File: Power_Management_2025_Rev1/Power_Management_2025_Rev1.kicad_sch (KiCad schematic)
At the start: 100 parts, among them J1 RJ45_LED_Shielded, Q1 BSS138, Q2 IPB180N10S4-02, Q3 IPB180N10S4-02, Q4 IPB180N10S4-02, U1 Teensy4.1_DEV-16771, U10 LT1910, U11 LT1910, U12 PKE3316ZPI, U13 PKE3316ZPI, U14 LT1910, U2 OKI-78SR-3.3_1.5-W36-C, U3 ACS756xCB-050B-PFF, U4 Opamp_Dual, U5 Opamp_Dual, U6 Opamp_Dual

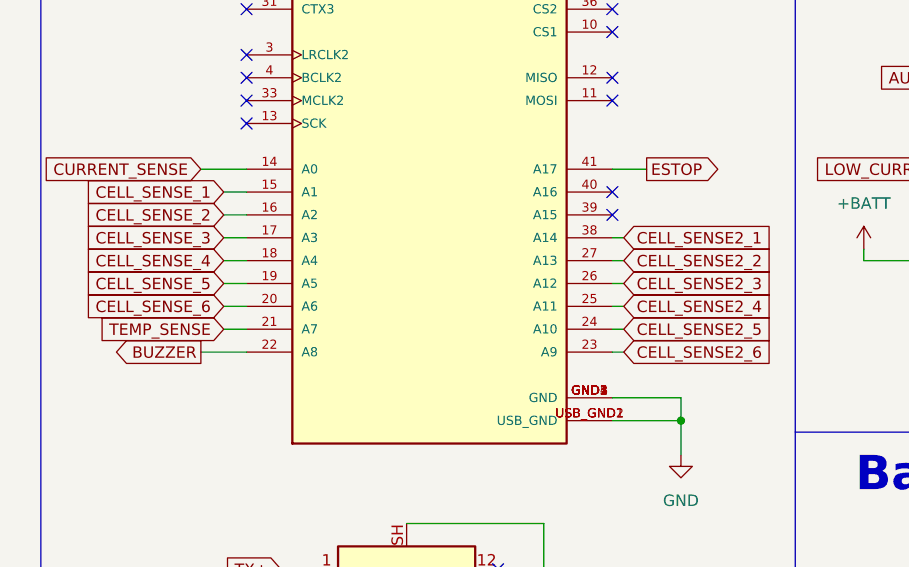
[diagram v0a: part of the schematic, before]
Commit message: Tracing
made a few more traces with the buzzer and cap bank
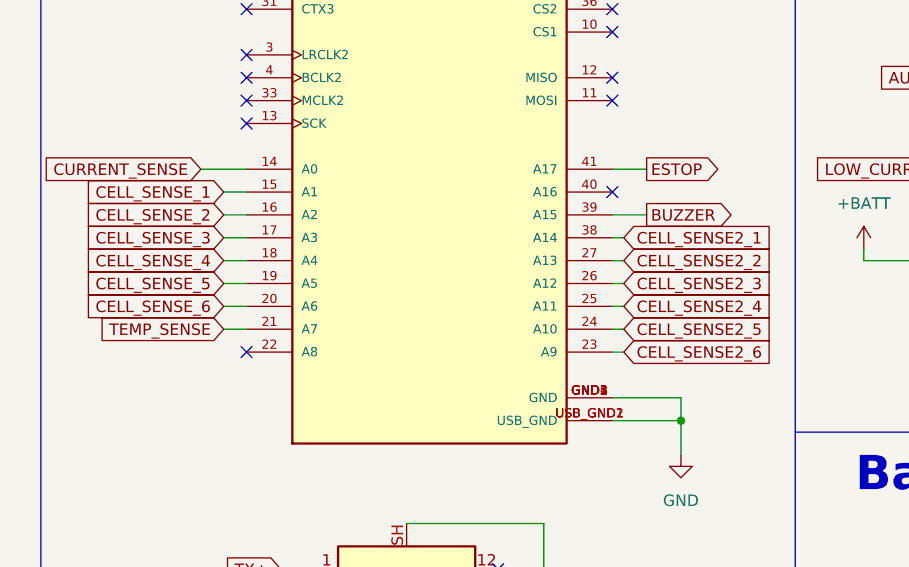
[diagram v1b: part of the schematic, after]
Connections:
- net BUZZER: now also U1.39 (A15); no longer U1.22 (A8)
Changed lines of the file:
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@@
 	)
 	(no_connect
-		(at 74.93 100.33)
-	)
-	(no_connect
 		(at 62.23 139.7)
 	)
@@
 	)
 	(no_connect
+		(at 34.29 115.57)
+	)
+	(no_connect
 		(at 74.93 57.15)
 	)
@@
 	(wire
 		(pts
+			(xy 74.93 100.33) (xy 78.74 100.33)
+		)
+		(stroke
+			(width 0)
+			(type default)
+		)
+	)
+	(wire
+		(pts
 			(xy 278.13 228.6) (xy 278.13 234.95)
 		)
@@
 	(wire
 		(pts
-			(xy 29.21 115.57) (xy 34.29 115.57)
-		)
-		(stroke
-			(width 0)
-			(type default)
-		)
-	)
-	(wire
-		(pts
 			(xy 337.82 224.79) (xy 336.55 224.79)
 		)
@@
 	(global_label "BUZZER"
 		(shape output)
-		(at 29.21 115.57 180)
+		(at 78.74 100.33 0)
 		(fields_autoplaced yes)
 		(effects
@@
 				(size 1.27 1.27)
 			)
-			(justify right)
+			(justify left)
 		)
 		(property "Intersheetrefs" "${INTERSHEET_REFS}"
-			(at 18.7863 115.57 0)
+			(at 89.1637 100.33 0)
 			(effects
 				(font
 					(size 1.27 1.27)
 				)
-				(justify right)
+				(justify left)
 				(hide yes)
 			)

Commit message: More tracework
Made corrections to schematic and did more tracework on PCB
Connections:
- net C_SENSE is gone; now on net CURRENT_SENSE: U3.3 (VIOUT)
- net +BATT: no longer C1.1, C12.1, C14.1, C9.1, F1.1, Q2.4 (D), Q3.4 (D), Q4.4 (D), R35.1, U10.6 (SENSE), U10.8 (V+), U11.6 (SENSE), U11.8 (V+), U12.3 (VIN+), U13.3 (VIN+), U14.6 (SENSE), U14.8 (V+), U2.1 (IN), U3.4 (IP+), U4.8 (V+), U5.8 (V+), U6.8 (V+)
- net IP+: now reaches C4.1, C5.1, C6.1, C7.1, D1.1 (K), F1.2
- net IP+: now also U3.4 (IP+)
- net FF_MOTOR: now reaches U1.22 (A8)
- net FF_MOTOR: now also R28.1
- net FF_LC: now reaches U1.40 (A16)
- net FF_LC: now also R27.1
- removed net +5V: R2.1, R27.1, R28.1
- net ESTOP renamed FF_AUX
- net FF_AUX: now also R2.1
- net PACK_OUT renamed IP-
- net IP-: now also C1.1, C12.1, C14.1, C9.1, F1.1, Q2.4 (D), Q3.4 (D), Q4.4 (D), R35.1, U10.6 (SENSE), U10.8 (V+), U11.6 (SENSE), U11.8 (V+), U12.3 (VIN+), U13.3 (VIN+), U14.6 (SENSE), U14.8 (V+), U2.1 (IN), U4.8 (V+), U5.8 (V+), U6.8 (V+)
- no-connect marks 37 -> 35
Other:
- moved on the sheet: C1, C12, C2, C9, Q2, Q4, U10, U14, U2

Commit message: Pushing opamp new numbers
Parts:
- R10, R11, R14, R15, R18, R19, R22, R23, R26, R4, R6, R7: value 36.5k -> 39k
- R12, R13, R16, R17, R20, R21, R24, R25, R3, R5, R8, R9: value 46.4k -> 47k
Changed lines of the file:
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@@
 			)
 		)
-		(property "Value" "36.5k"
+		(property "Value" "39k"
 			(at 203.2 190.754 90)
 			(effects
@@
 			)
 		)
-		(property "Value" "36.5k"
+		(property "Value" "39k"
 			(at 272.034 177.8 90)
 			(effects
@@
 			)
 		)
-		(property "Value" "46.4k"
+		(property "Value" "47k"
 			(at 292.1 197.104 90)
 			(effects
@@
 			)
 		)
-		(property "Value" "46.4k"
+		(property "Value" "47k"
 			(at 115.824 189.484 90)
 			(effects
@@
 			)
 		)
-		(property "Value" "46.4k"
+		(property "Value" "47k"
 			(at 214.63 190.5 90)
 			(effects
@@
 			)
 		)
-		(property "Value" "46.4k"
+		(property "Value" "47k"
 			(at 252.73 192.024 90)
 			(effects
@@
 			)
 		)
-		(property "Value" "46.4k"
+		(property "Value" "47k"
 			(at 182.88 193.294 90)
 			(effects
@@
 			)
 		)
-		(property "Value" "36.5k"
+		(property "Value" "39k"
 			(at 306.07 179.324 90)
 			(effects
@@
 			)
 		)
-		(property "Value" "36.5k"
+		(property "Value" "39k"
 			(at 196.85 176.784 90)
 			(effects
@@
 			)
 		)
-		(property "Value" "46.4k"
+		(property "Value" "47k"
 			(at 287.02 194.564 90)
 			(effects
@@
 			)
 		)
-		(property "Value" "36.5k"
+		(property "Value" "39k"
 			(at 166.37 189.23 90)
 			(effects
@@
 			)
 		)
-		(property "Value" "46.4k"
+		(property "Value" "47k"
 			(at 145.034 188.214 90)
 			(effects
@@
 			)
 		)
-		(property "Value" "46.4k"
+		(property "Value" "47k"
 			(at 177.8 190.754 90)
 			(effects
@@
 			)
 		)
-		(property "Value" "36.5k"
+		(property "Value" "39k"
 			(at 233.68 176.53 90)
 			(effects
@@
 			)
 		)
-		(property "Value" "36.5k"
+		(property "Value" "39k"
 			(at 275.844 193.294 90)
 			(effects
@@
 			)
 		)
-		(property "Value" "46.4k"
+		(property "Value" "47k"
 			(at 219.71 193.294 90)
 			(effects
@@
 			)
 		)
-		(property "Value" "36.5k"
+		(property "Value" "39k"
 			(at 129.794 172.974 90)
 			(effects
@@
 			)
 		)
-		(property "Value" "46.4k"
+		(property "Value" "47k"
 			(at 149.86 190.754 90)
 			(effects
@@
 			)
 		)
-		(property "Value" "46.4k"
+		(property "Value" "47k"
 			(at 257.81 194.564 90)
 			(effects
@@
 			)
 		)
-		(property "Value" "36.5k"
+		(property "Value" "39k"
 			(at 241.3 192.024 90)
 			(effects
@@
 			)
 		)
-		(property "Value" "46.4k"
+		(property "Value" "47k"
 			(at 110.744 186.944 90)
 			(effects
@@
 			)
 		)
-		(property "Value" "36.5k"
+		(property "Value" "39k"
 			(at 133.604 188.214 90)
 			(effects
@@
 			)
 		)
-		(property "Value" "36.5k"
+		(property "Value" "39k"
 			(at 99.314 186.944 90)
 			(effects
@@
 			)
 		)
-		(property "Value" "36.5k"
+		(property "Value" "39k"
 			(at 163.83 174.244 90)
 			(effects

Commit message: Rearranged component
We Made power planes
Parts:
- C1, C11, C12, C13, C14, C2, C9: footprint Capacitor_THT:CP_Radial_D5.0mm_P2.00mm -> Capacitor_SMD:C_1206_3216Metric_Pad1.33x1.80mm_HandSolder
- C10, C8: footprint Capacitor_THT:CP_Radial_Tantal_D5.0mm_P5.00mm -> Capacitor_THT:CP_Radial_D5.0mm_P2.00mm
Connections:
- net +BATT is gone; now on net IP+: Conn1.4 (PV+), Conn19.4 (PV+)
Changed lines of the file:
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@@
 		)
 	)
+	(global_label "IP+"
+		(shape output)
+		(at 33.02 189.23 90)
+		(fields_autoplaced yes)
+		(effects
+			(font
+				(size 1.27 1.27)
+			)
+			(justify left)
+		)
+		(property "Intersheetrefs" "${INTERSHEET_REFS}"
+			(at 33.02 182.7976 90)
+			(effects
+				(font
+					(size 1.27 1.27)
+				)
+				(justify left)
+				(hide yes)
+			)
+		)
+	)
 	(global_label "CELL4"
 		(shape input)
@@
 		)
 	)
+	(global_label "IP+"
+		(shape output)
+		(at 59.69 187.96 90)
+		(fields_autoplaced yes)
+		(effects
+			(font
+				(size 1.27 1.27)
+			)
+			(justify left)
+		)
+		(property "Intersheetrefs" "${INTERSHEET_REFS}"
+			(at 59.69 181.5276 90)
+			(effects
+				(font
+					(size 1.27 1.27)
+				)
+				(justify left)
+				(hide yes)
+			)
+		)
+	)
 	(global_label "BUZZER"
 		(shape output)
@@
 			)
 		)
-		(property "Footprint" "Capacitor_THT:CP_Radial_D5.0mm_P2.00mm"
+		(property "Footprint" "Capacitor_SMD:C_1206_3216Metric_Pad1.33x1.80mm_HandSolder"
 			(at 372.11 241.3 0)
 			(effects
@@
 			)
 		)
-		(property "Footprint" "Capacitor_THT:CP_Radial_D5.0mm_P2.00mm"
+		(property "Footprint" "Capacitor_SMD:C_1206_3216Metric_Pad1.33x1.80mm_HandSolder"
 			(at 307.0352 48.26 0)
 			(effects
@@
 			)
 		)
-		(property "Footprint" "Capacitor_THT:CP_Radial_D5.0mm_P2.00mm"
+		(property "Footprint" "Capacitor_SMD:C_1206_3216Metric_Pad1.33x1.80mm_HandSolder"
 			(at 278.13 260.35 0)
 			(effects
@@
 			)
 		)
-		(property "Footprint" "Capacitor_THT:CP_Radial_D5.0mm_P2.00mm"
+		(property "Footprint" "Capacitor_SMD:C_1206_3216Metric_Pad1.33x1.80mm_HandSolder"
 			(at 322.2752 48.26 0)
 			(effects
@@
 			)
 		)
-		(property "Footprint" "Capacitor_THT:CP_Radial_Tantal_D5.0mm_P5.00mm"
+		(property "Footprint" "Capacitor_THT:CP_Radial_D5.0mm_P2.00mm"
 			(at 360.9848 96.52 0)
 			(effects
@@
 	)
 	(symbol
-		(lib_id "power:+BATT")
-		(at 33.02 189.23 0)
-		(unit 1)
-		(exclude_from_sim no)
-		(in_bom yes)
-		(on_board yes)
-		(dnp no)
-		(fields_autoplaced yes)
-		(property "Reference" "#PWR01"
-			(at 33.02 193.04 0)
-			(effects
-				(font
-					(size 1.27 1.27)
-				)
-				(hide yes)
-			)
-		)
-		(property "Value" "+BATT"
-			(at 33.02 184.15 0)
-			(effects
-				(font
-					(size 1.27 1.27)
-				)
-			)
-		)
-		(property "Footprint" ""
-			(at 33.02 189.23 0)
-			(effects
-				(font
-					(size 1.27 1.27)
-				)
-				(hide yes)
-			)
-		)
-		(property "Datasheet" ""
-			(at 33.02 189.23 0)
-			(effects
-				(font
-					(size 1.27 1.27)
-				)
-				(hide yes)
-			)
-		)
-		(property "Description" "Power symbol creates a global label with name \"+BATT\""
-			(at 33.02 189.23 0)
-			(effects
-				(font
-					(size 1.27 1.27)
-				)
-				(hide yes)
-			)
-		)
-		(pin "1"
-		)
-		(instances
-			(project ""
-				(path "/e068baf1-d1f0-499a-9461-2503f4f0f679"
-					(reference "#PWR01")
-					(unit 1)
-				)
-			)
-		)
-	)
-	(symbol
 		(lib_id "MRDT_Connectors:AndersonPP")
 		(at 201.93 50.8 0)
@@
 			)
 		)
-		(property "Footprint" "Capacitor_THT:CP_Radial_Tantal_D5.0mm_P5.00mm"
+		(property "Footprint" "Capacitor_THT:CP_Radial_D5.0mm_P2.00mm"
 			(at 354.6348 163.83 0)
 			(effects
@@
 			)
 		)
-		(property "Footprint" "Capacitor_THT:CP_Radial_D5.0mm_P2.00mm"
+		(property "Footprint" "Capacitor_SMD:C_1206_3216Metric_Pad1.33x1.80mm_HandSolder"
 			(at 336.8548 163.83 0)
 			(effects
@@
 			)
 		)
-		(property "Footprint" "Capacitor_THT:CP_Radial_D5.0mm_P2.00mm"
+		(property "Footprint" "Capacitor_SMD:C_1206_3216Metric_Pad1.33x1.80mm_HandSolder"
 			(at 199.39 261.62 0)
 			(effects
@@
 	)
 	(symbol
-		(lib_id "power:+BATT")
-		(at 59.69 187.96 0)
-		(unit 1)
-		(exclude_from_sim no)
-		(in_bom yes)
-		(on_board yes)
-		(dnp no)
-		(fields_autoplaced yes)
-		(property "Reference" "#PWR061"
-			(at 59.69 191.77 0)
-			(effects
-				(font
-					(size 1.27 1.27)
-				)
-				(hide yes)
-			)
-		)
-		(property "Value" "+BATT"
-			(at 59.69 182.88 0)
-			(effects
-				(font
-					(size 1.27 1.27)
-				)
-			)
-		)
-		(property "Footprint" ""
-			(at 59.69 187.96 0)
-			(effects
-				(font
-					(size 1.27 1.27)
-				)
-				(hide yes)
-			)
-		)
-		(property "Datasheet" ""
-			(at 59.69 187.96 0)
-			(effects
-				(font
-					(size 1.27 1.27)
-				)
-				(hide yes)
-			)
-		)
-		(property "Description" "Power symbol creates a global label with name \"+BATT\""
-			(at 59.69 187.96 0)
-			(effects
-				(font
-					(size 1.27 1.27)
-				)
-				(hide yes)
-			)
-		)
-		(pin "1"
-		)
-		(instances
-			(project "Power_Management_2025_Rev1"
-				(path "/e068baf1-d1f0-499a-9461-2503f4f0f679"
-					(reference "#PWR061")
-					(unit 1)
-				)
-			)
-		)
-	)
-	(symbol
 		(lib_id "Device:R")
 		(at 133.35 185.42 0)
@@
 			)
 		)
-		(property "Footprint" "Capacitor_THT:CP_Radial_D5.0mm_P2.00mm"
+		(property "Footprint" "Capacitor_SMD:C_1206_3216Metric_Pad1.33x1.80mm_HandSolder"
 			(at 349.5548 96.52 0)
 			(effects

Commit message: Schematic save
Schematic save
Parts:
- U10, U11, U14: footprint Package_SO:SOIC-8-N7_3.9x4.9mm_P1.27mm -> Package_SO:SOIC-8_3.9x4.9mm_P1.27mm
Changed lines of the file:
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@@
 			)
 		)
-		(property "Footprint" "Package_SO:SOIC-8-N7_3.9x4.9mm_P1.27mm"
+		(property "Footprint" "Package_SO:SOIC-8_3.9x4.9mm_P1.27mm"
 			(at 345.44 234.95 0)
 			(effects
@@
 			)
 		)
-		(property "Footprint" "Package_SO:SOIC-8-N7_3.9x4.9mm_P1.27mm"
+		(property "Footprint" "Package_SO:SOIC-8_3.9x4.9mm_P1.27mm"
 			(at 172.72 255.27 0)
 			(effects
@@
 			)
 		)
-		(property "Footprint" "Package_SO:SOIC-8-N7_3.9x4.9mm_P1.27mm"
+		(property "Footprint" "Package_SO:SOIC-8_3.9x4.9mm_P1.27mm"
 			(at 251.46 254 0)
 			(effects

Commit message: Worked on corrections
Retraced opamp circuit, fixed diff pair, moved capacitors to be closer to what they filter, increased size of silkscreens, fixed inputs and outputs in relation to opamps and teensie
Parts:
- U2: footprint Converter_DCDC:Converter_DCDC_Murata_OKI-78SR_Vertical -> Converter_DCDC:Converter_DCDC_Murata_OKI-78SR_Horizontal
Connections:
- net +3.3V: now also R2.1, R27.1, R28.1
- net CELL1: now also Conn2.6, Conn20.6
- net CELL2: now also Conn2.5, Conn20.5
- net CELL3: now also Conn2.4, Conn20.4
- net CELL4: now also Conn2.3, Conn20.3
- net CELL5: now also Conn2.2, Conn20.2
- net CELL6: now also Conn2.1, Conn20.1
- net CELL_SENSE_1: no longer Conn2.6
- net CELL_SENSE_2: no longer Conn2.5
- net CELL_SENSE_3: no longer Conn2.4
- net CELL_SENSE_4: no longer Conn2.3
- net CELL_SENSE_5: no longer Conn2.2
- net CELL_SENSE_6: no longer Conn2.1
- net IP+: now also F1.1; no longer C4.1, C5.1, C6.1, C7.1, D1.1 (K), F1.2
- net IP-: now also C4.1, C5.1, C6.1, C7.1, D1.1 (K), F1.2; no longer F1.1
- net CELL_SENSE2_1: no longer names the net of U1.38 (A14)
- net CELL_SENSE2_1: no longer Conn20.6
- net CELL_SENSE2_2: no longer names the net of U1.27 (A13)
- net CELL_SENSE2_2: no longer Conn20.5
- net CELL_SENSE2_3: no longer names the net of U1.26 (A12)
- net CELL_SENSE2_3: no longer Conn20.4
- net CELL_SENSE2_4: no longer names the net of U1.25 (A11)
- net CELL_SENSE2_4: no longer Conn20.3
- net CELL_SENSE2_5: no longer names the net of U1.24 (A10)
- net CELL_SENSE2_5: no longer Conn20.2
- net CELL_SENSE2_6: no longer names the net of U1.23 (A9)
- net CELL_SENSE2_6: no longer Conn20.1
- net FF_AUX: no longer names the net of U1.41 (A17)
- net FF_AUX: no longer R2.1
- net FF_LC: no longer names the net of U1.40 (A16)
- net FF_LC: no longer R27.1
- net FF_MOTOR: no longer names the net of U1.22 (A8)
- net FF_MOTOR: no longer R28.1
- no-connect marks 35 -> 44

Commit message: We changed the planes
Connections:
- net IP-: no longer C4.1, C5.1, C6.1, C7.1, D1.1 (K), F1.2
- net IP+ renamed PV+
- net PV+: no longer U3.4 (IP+)
- new net PV-: C4.1, C5.1, C6.1, C7.1, D1.1 (K), F1.2, U3.4 (IP+)

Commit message: Few board rev changes
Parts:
- U2: footprint Converter_DCDC:Converter_DCDC_Murata_OKI-78SR_Horizontal -> MRDT_Devices:OKI_Horizontal
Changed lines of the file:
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@@
 			)
 		)
-		(property "Footprint" "Converter_DCDC:Converter_DCDC_Murata_OKI-78SR_Horizontal"
+		(property "Footprint" "MRDT_Devices:OKI_Horizontal"
 			(at 314.96 46.99 0)
 			(effects
